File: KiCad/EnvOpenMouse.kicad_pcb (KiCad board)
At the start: 2 copper layers, 52.3 x 30.4 mm, 24 parts, among them J1 Conn_01x08, J2 Conn_01x03, J3 Conn_01x03, J4 Conn_01x03, SW1 SW_Push_SPDT, SW2 SW_Push_SPDT, U1 TCR2EF19, U2 PMW3360DM-T2QU

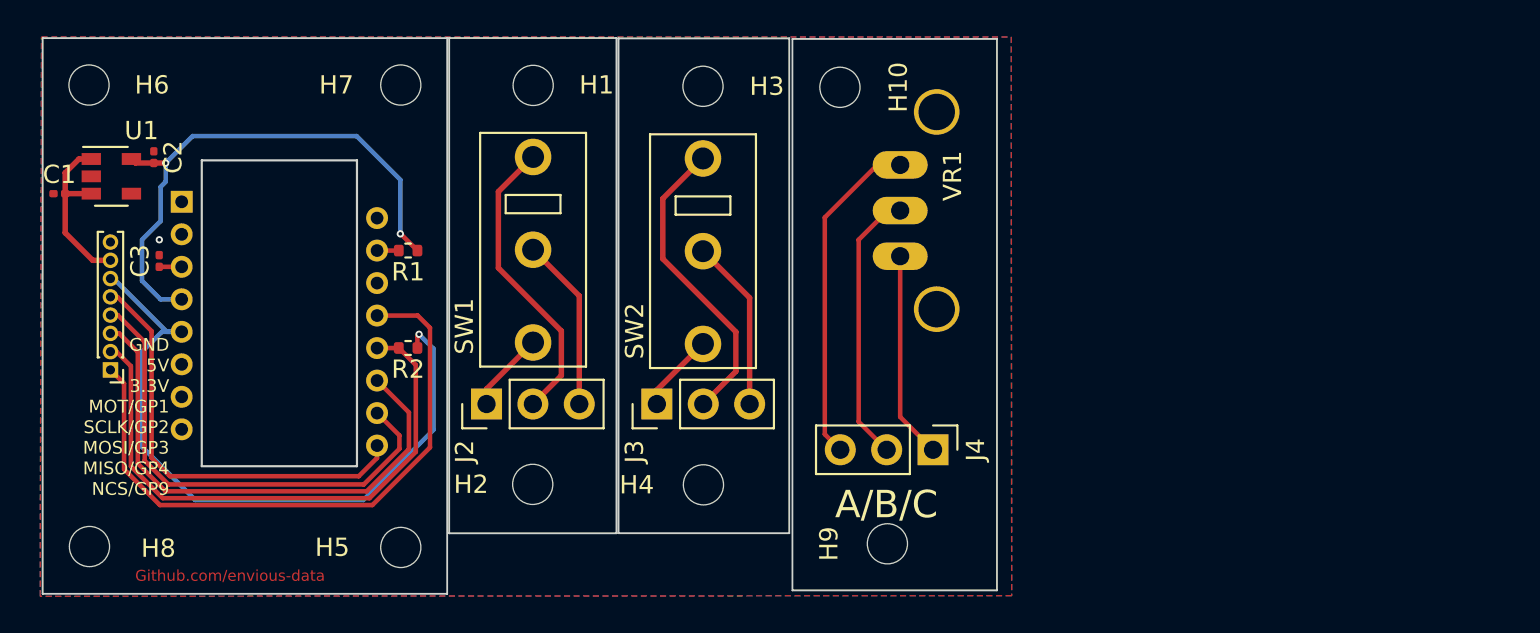
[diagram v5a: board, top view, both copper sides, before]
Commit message: added missing capactor and middle click button.
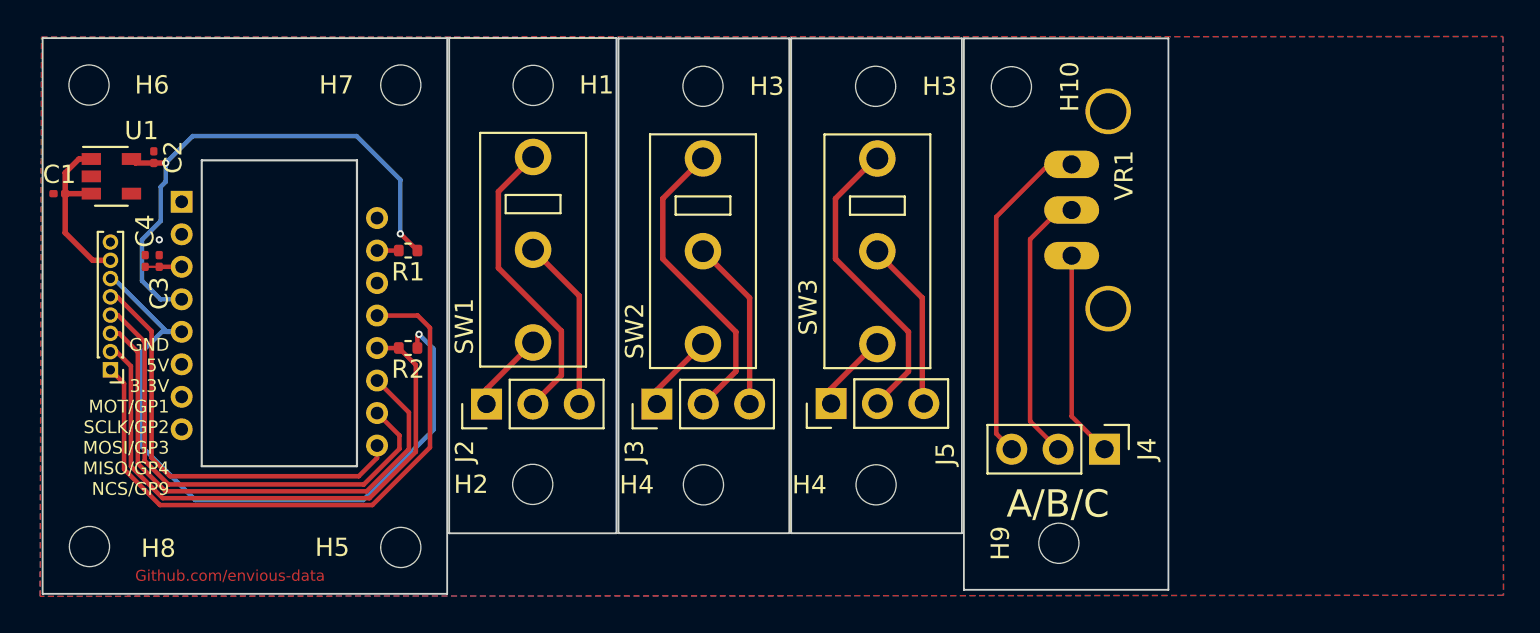
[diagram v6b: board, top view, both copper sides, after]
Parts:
- added C4: 100nf 0402, Capacitor_SMD:C_0201_0603Metric, F.Cu at (19.4, 24.6)
- added H3: MountingHole_Pad, MountingHole:MountingHole_2.2mm_M2, F.Cu at (59.5, 15.0)
- added H4: MountingHole_Pad, MountingHole:MountingHole_2.2mm_M2, F.Cu at (59.5, 36.8)
- added J5: Conn_01x03, Connector_PinHeader_2.54mm:PinHeader_1x03_P2.54mm_Vertical, F.Cu at (57.0, 32.4)
- added SW3: SW_Push_SPDT, MouseSwitch:MouseSwitch, F.Cu at (59.5, 24.0)
- moved H10 9.39 mm to (66.9, 15.0)
- moved VR1 9.39 mm to (70.2, 21.8)
- moved H9 9.39 mm to (69.5, 40.0)
- moved J4 9.39 mm to (72.0, 34.9)
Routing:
- net Net-(J5-Pad2): track 0.00 -> 16.8 mm
- net Net-(J5-Pad3): track 0.00 -> 9.43 mm
- net Net-(J5-Pad1): track 0.00 -> 4.34 mm
- net Net-(C3-Pad1): track 1.23 -> 2.00 mm
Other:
- board size 52.3 x 30.4 mm -> 61.7 x 30.4 mm

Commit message: Appended RP2040 to board, begin work on Mouse PCB
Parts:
- removed H10, H5, H6, H7, H8, H9: MountingHole_Pad, MountingHole:MountingHole_2.2mm_M2
- removed the H3 at (59.5, 15.0)
- removed the H3 at (50.0, 15.0)
- removed the H4 at (50.0, 36.8)
- removed the H4 at (59.5, 36.8)
- added C10: 100nf 0402, Capacitor_SMD:C_0402_1005Metric, F.Cu at (80.7, 85.0)
- added C11: 100nf 0402, Capacitor_SMD:C_0402_1005Metric, F.Cu at (77.8, 85.0)
- added C12: 100nf 0402, Capacitor_SMD:C_0402_1005Metric, F.Cu at (77.8, 87.0)
- added C13: 100nf 0402, Capacitor_SMD:C_0402_1005Metric, F.Cu at (66.9, 87.0)
- added C14: 100nf 0402, Capacitor_SMD:C_0402_1005Metric, F.Cu at (72.0, 85.7)
- added C15: 100nf 0402, Capacitor_SMD:C_0402_1005Metric, F.Cu at (80.0, 81.1)
- added C16: 100nf 0402, Capacitor_SMD:C_0402_1005Metric, F.Cu at (80.0, 83.1)
- added C17: 1uf 0402, Capacitor_SMD:C_0402_1005Metric, F.Cu at (72.0, 83.7)
- added C18: 1uf 0402, Capacitor_SMD:C_0402_1005Metric, F.Cu at (69.8, 87.6)
- added C19: 100nf 0402, Capacitor_SMD:C_0402_1005Metric, F.Cu at (61.2, 89.0)
- added C20: 10uf 0402, Capacitor_SMD:C_0402_1005Metric, F.Cu at (82.9, 82.2)
- added C21: 22pf 0402, Capacitor_SMD:C_0402_1005Metric, F.Cu at (64.0, 88.8)
- added C22: 22pf 0402, Capacitor_SMD:C_0402_1005Metric, F.Cu at (69.8, 89.6)
- added C5: 10uf 0402, Capacitor_SMD:C_0402_1005Metric, F.Cu at (69.2, 84.1)
- added C6: 10uf 0402, Capacitor_SMD:C_0402_1005Metric, F.Cu at (72.6, 87.6)
- added C7: 0.1uf 0402, Capacitor_SMD:C_0402_1005Metric, F.Cu at (66.9, 89.0)
- added C8: 100nf 0402, Capacitor_SMD:C_0402_1005Metric, F.Cu at (74.9, 85.7)
- added C9: 100nf 0402, Capacitor_SMD:C_0402_1005Metric, F.Cu at (74.9, 83.7)
- added CBP1: 10uf 0402, Capacitor_SMD:C_0402_1005Metric, F.Cu at (66.3, 85.0)
- added D1: 1N4002W, Diode_SMD:D_SOD-123, F.Cu at (51.6, 90.3)
- added F1: 0805L050WR, Fuse:Fuse_0805_2012Metric, F.Cu at (76.6, 74.7)
- added FB1: FerriteBead 0402, Resistor_SMD:R_0402_1005Metric, F.Cu at (77.1, 81.1)
- added FLASH1: W25Q16JVUXIQ, Package_SON:SON-8-1EP_3x2mm_P0.5mm_EP1.4x1.6mm, F.Cu at (72.1, 75.0)
- added GP23_LED1: GP23 LED_0402, LED_SMD:LED_0402_1005Metric, F.Cu at (84.5, 74.2)
- added GPIO24_RESISTOR1: 1K 0402, Resistor_SMD:R_0402_1005Metric, F.Cu at (68.4, 82.2)
- added GPIO25_LED1: LED_0402, LED_SMD:LED_0402_1005Metric, F.Cu at (87.7, 74.2)
- added GPIO25_RESISTOR1: 470 0402, Resistor_SMD:R_0402_1005Metric, F.Cu at (83.1, 78.2)
- added H3: MountingHole_Pad, MountingHole:MountingHole_2.2mm_M2, F.Cu at (122.8, 156.7)
- added H4: MountingHole_Pad, MountingHole:MountingHole_2.2mm_M2, F.Cu at (122.8, 162.6)
- added J8: TSA343G00-250J2, Button_Switch_SMD:SW_Push_SPST_NO_Alps_SKRK, F.Cu at (46.2, 85.1)
- added J9: Conn_01x03_Male, Connector_PinHeader_2.54mm:PinHeader_1x03_P2.54mm_Vertical, F.Cu at (55.9, 75.5)
- added NT1: NetTie_2, NetTie:NetTie-2_SMD_Pad0.5mm, F.Cu at (84.4, 76.2)
- added Q1: SI2301B, Package_TO_SOT_SMD:SOT-23, F.Cu at (67.3, 75.4)
- added R10: 10K 0402, Resistor_SMD:R_0402_1005Metric, F.Cu at (74.2, 81.7)
- added R11: 27r 0402 resistor, Resistor_SMD:R_0402_1005Metric, F.Cu at (77.3, 77.1)
- added R12: 27r 0402 resistor, Resistor_SMD:R_0402_1005Metric, F.Cu at (80.2, 77.1)
- added R13: 10K 0402, Resistor_SMD:R_0402_1005Metric, F.Cu at (71.5, 77.7)
- added R14: 1K 0402, Resistor_SMD:R_0402_1005Metric, F.Cu at (74.4, 77.7)
- added R15: 1K 0402, Resistor_SMD:R_0402_1005Metric, F.Cu at (65.5, 82.2)
- added R3: 5.1K 0402, Resistor_SMD:R_0402_1005Metric, F.Cu at (86.0, 79.2)
- added R4: 200 0603, Resistor_SMD:R_0603_1608Metric, F.Cu at (80.8, 74.4)
- added R5: 5.6K 0402, Resistor_SMD:R_0402_1005Metric, F.Cu at (71.3, 81.6)
- added R6: 1 0402, Resistor_SMD:R_0402_1005Metric, F.Cu at (83.1, 80.2)
- added R7: 5.1K 0402, Resistor_SMD:R_0402_1005Metric, F.Cu at (77.3, 79.1)
- added R8: 100K 0402, Resistor_SMD:R_0402_1005Metric, F.Cu at (80.2, 79.1)
- added R9: 220 0402, Resistor_SMD:R_0402_1005Metric, F.Cu at (74.2, 79.7)
- added RSW1: TSA343G00-250J2, Button_Switch_SMD:SW_Push_SPST_NO_Alps_SKRK, F.Cu at (61.5, 75.4)
- added TP1: TestPoint, EnvExtras:CustomTestPoint, F.Cu at (87.4, 76.7)
- added TP2: TestPoint, EnvExtras:CustomTestPoint, F.Cu at (68.5, 79.1)
- added TP3: TestPoint, EnvExtras:CustomTestPoint, F.Cu at (65.5, 79.7)
- added U3: SOT-23-5 5.5V 3.3V 500mA, Package_TO_SOT_SMD:SOT-23-5, F.Cu at (62.3, 85.6)
- added U4: RP2040, RP2040_minimal:RP2040-QFN-56, F.Cu at (38.3, 130.7)
- added USB1: TYPE-C-31-M-12, HRO-TYPE-C31-M-12:HRO-TYPE-C-31-M-12, F.Cu at (48.3, 82.1)
- added Y1: 3225_4P, Crystal:Crystal_SMD_3225-4Pin_3.2x2.5mm, F.Cu at (57.1, 90.8)
- C3: value 4.7uf 0402 -> 100nf 0402
- C4: value 100nf 0402 -> 4.7uf 0402
- U1: value TCR2EF19 -> TLV70218DBVR
- moved H1 166.1 mm to (116.8, 162.6)
- moved J3 144.6 mm to (92.1, 169.9)
- moved SW2 144.6 mm to (94.7, 161.5)
- moved H2 142.0 mm to (116.8, 156.7)
- moved C1 134.6 mm to (25.4, 155.0)
- moved C2 134.6 mm to (30.5, 153.0)
- moved C3 134.6 mm to (30.8, 158.7)
- moved C4 134.6 mm to (30.1, 158.7)
- moved J1 134.6 mm to (28.1, 164.7)
- moved R2 134.6 mm to (44.5, 163.5)
- moved R1 134.6 mm to (44.5, 158.1)
- moved U1 134.6 mm to (28.2, 154.1)
- moved U2 134.6 mm to (33.1, 153.9)
- moved J2 133.8 mm to (53.9, 165.3)
- moved SW1 133.8 mm to (56.5, 156.8)
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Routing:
- removed copper zone on B.Cu, net GND
- removed copper zone on F.Cu, net GND
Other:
- board size 61.7 x 30.4 mm -> 8.5 x 16.8 mm
- board text removed: "Github.com/envious-data"

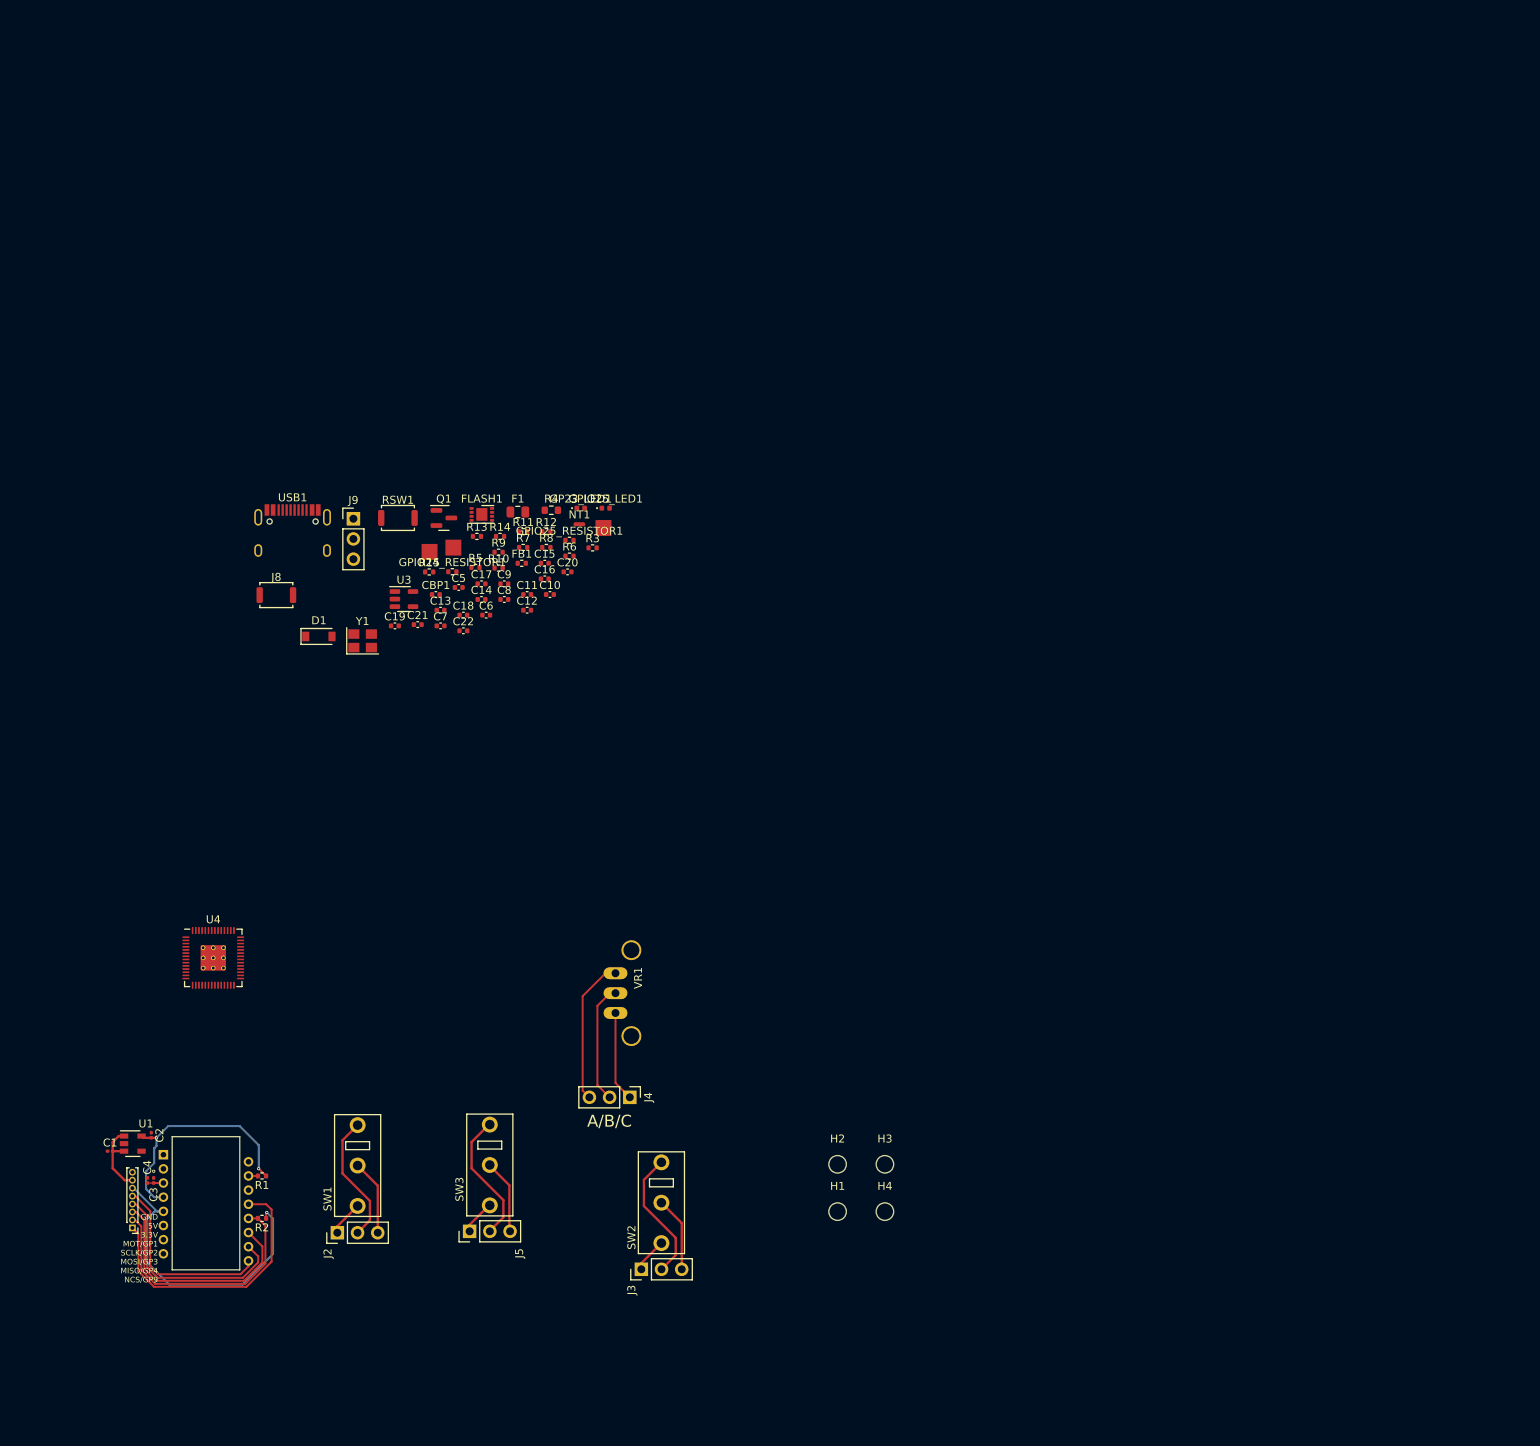
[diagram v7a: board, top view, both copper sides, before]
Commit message: routed onboard MCU
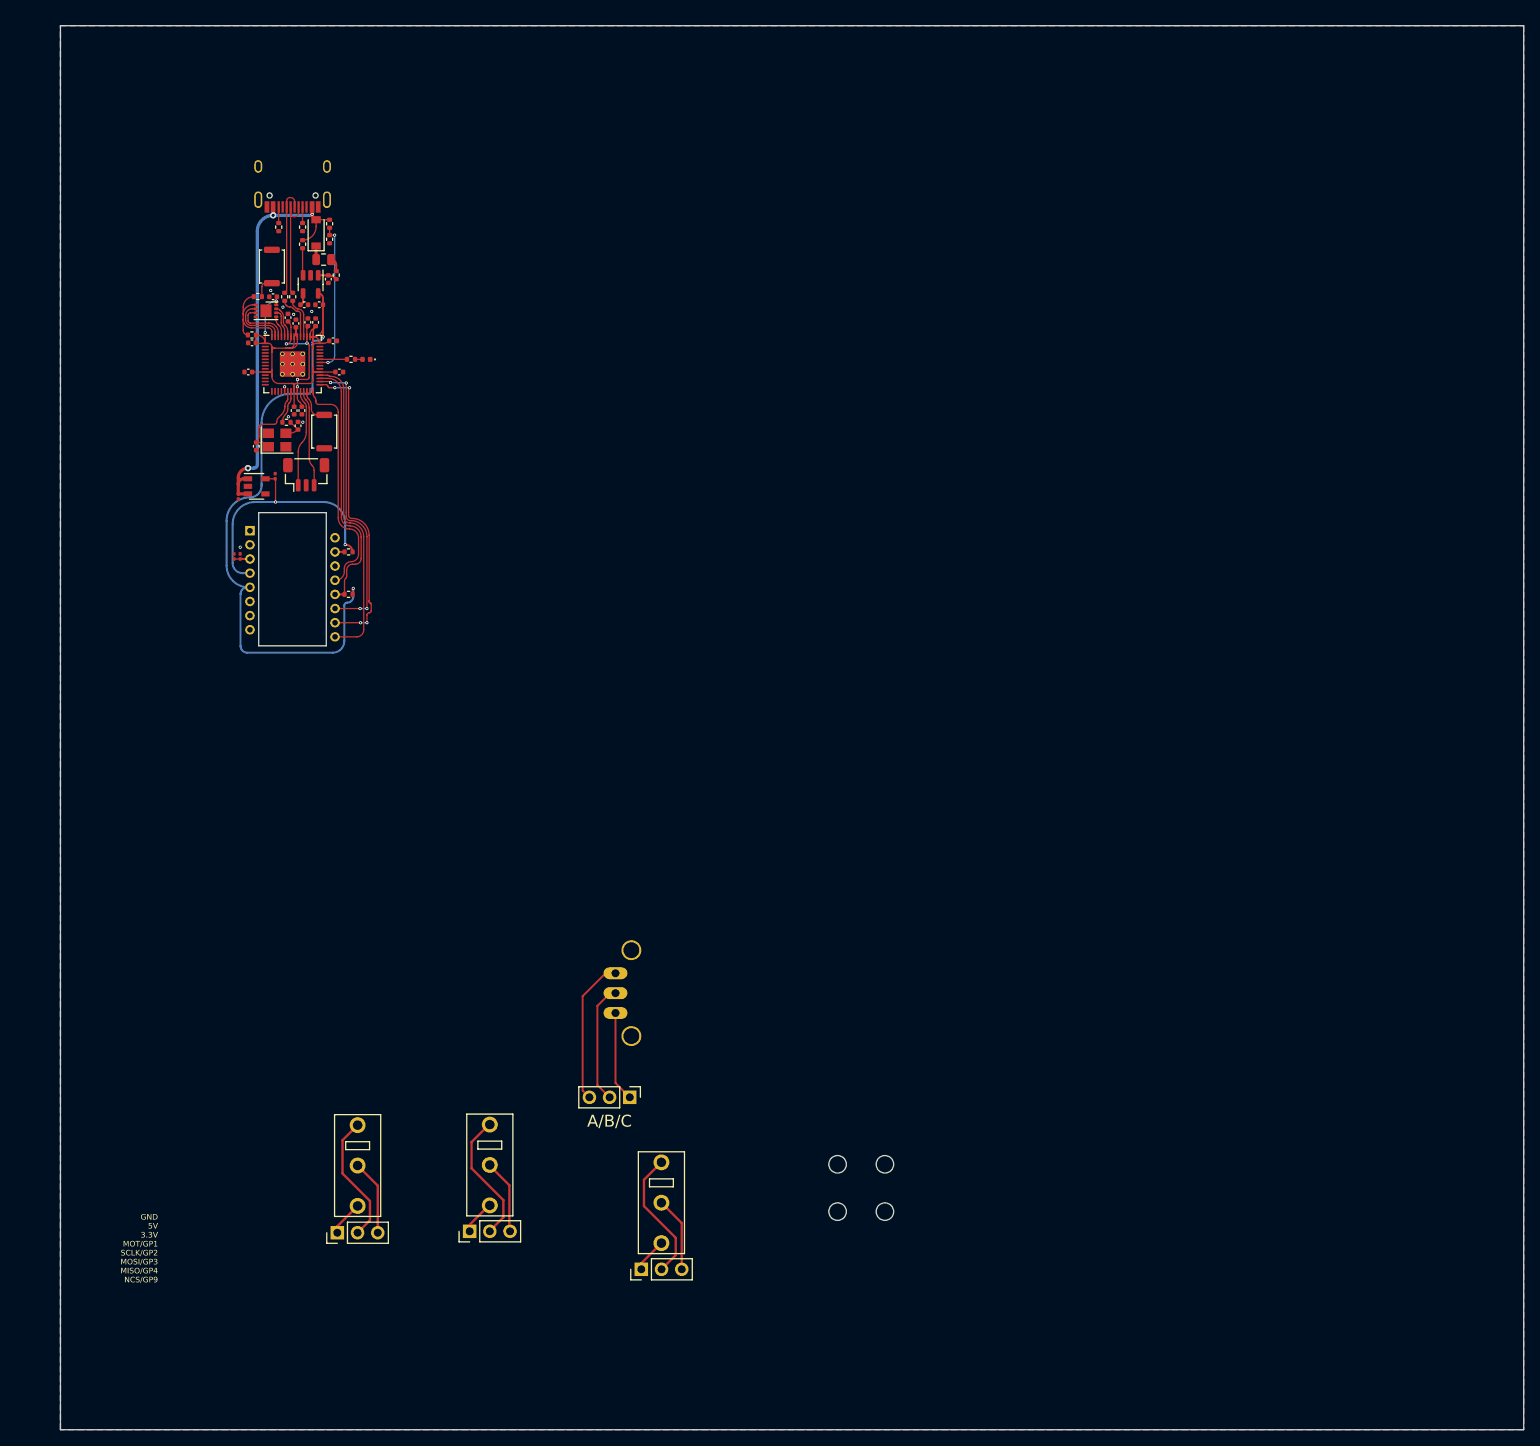
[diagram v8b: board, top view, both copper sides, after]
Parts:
- removed C16: 100nf 0402, Capacitor_SMD:C_0402_1005Metric
- removed C20: 10uf 0402, Capacitor_SMD:C_0402_1005Metric
- removed C7: 0.1uf 0402, Capacitor_SMD:C_0402_1005Metric
- removed GP23_LED1: GP23 LED_0402, LED_SMD:LED_0402_1005Metric
- removed GPIO24_RESISTOR1: 1K 0402, Resistor_SMD:R_0402_1005Metric
- removed J1: Conn_01x08, Connector_PinHeader_1.00mm:PinHeader_1x08_P1.00mm_Vertical
- removed NT1: NetTie_2, NetTie:NetTie-2_SMD_Pad0.5mm
- removed Q1: SI2301B, Package_TO_SOT_SMD:SOT-23
- removed R4: 200 0603, Resistor_SMD:R_0603_1608Metric
- removed R6: 1 0402, Resistor_SMD:R_0402_1005Metric
- removed R9: 220 0402, Resistor_SMD:R_0402_1005Metric
- removed TP1, TP2, TP3: TestPoint, EnvExtras:CustomTestPoint
- J9: value Conn_01x03_Male -> C145960; footprint Connector_PinHeader_2.54mm:PinHeader_1x03_P2.54mm_Vertical -> Connector_JST:JST_SH_BM03B-SRSS-TB_1x03-1MP_P1.00mm_Vertical
- moved C2 84.3 mm to (46.1, 70.2)
- moved U1 84.1 mm to (43.8, 71.4)
- moved C1 83.9 mm to (41.5, 72.7), turned to 90 degrees
- moved C3 79.2 mm to (41.7, 80.2)
- moved C4 79.2 mm to (40.9, 80.2)
- moved R1 79.2 mm to (55.3, 79.7)
- moved R2 79.2 mm to (55.3, 85.0)
- moved U2 79.2 mm to (44.0, 75.5)
- moved U4 75.3 mm to (48.3, 56.0)
- moved R3 54.4 mm to (49.5, 38.8), turned to 90 degrees
- moved USB1 53.5 mm to (48.3, 28.6), turned to 180 degrees
- moved D1 50.8 mm to (51.2, 39.5), turned to 90 degrees
- moved R7 50.7 mm to (46.5, 38.8), turned to 90 degrees
- moved R8 48.9 mm to (49.5, 41.0), turned to 90 degrees
- moved R5 46.9 mm to (53.0, 38.4), turned to -90 degrees
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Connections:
- C1 pad 2: +5V -> VBUS
- U1 pad 1: +5V -> VBUS
- U1 pad 3: +5V -> VBUS
- U4 pad 28: /RP2040/GPIO17 -> NCS/GPIO9
- U4 pad 29: /RP2040/GPIO18 -> SCLK/GPIO2
- U4 pad 30: /RP2040/GPIO19 -> MOSI/GPIO3
- U4 pad 31: /RP2040/GPIO20 -> MISO/GPIO4
- U4 pad 32: /RP2040/GPIO21 -> MOTION/GPIO1
- USB1 pad 13: Net-(C7-Pad2) -> GND
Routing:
- net +3V3: track 38.0 -> 139.5 mm, vias 1 -> 4
- net VBUS: track 0.00 -> 55.3 mm, vias 0 -> 3
- net /RP2040/GPIO24: track 0.00 -> 19.0 mm, vias 0 -> 2
- net +1V1: track 0.00 -> 17.7 mm, vias 0 -> 4
- net MOTION/GPIO1: track 23.8 -> 39.6 mm
- net USB_D-: track 0.00 -> 13.9 mm
- net USB_D+: track 0.00 -> 13.8 mm
- net /RP2040/QSPI_SS: track 0.00 -> 13.1 mm
- net SCLK/GPIO2: track 26.7 -> 39.7 mm, vias 0 -> 4
- net /RP2040/SWCLK: track 0.00 -> 12.3 mm
- net /RP2040/SWD: track 0.00 -> 12.1 mm
- net XIN: track 0.00 -> 10.6 mm
- net +5V: track 9.57 -> 0.00 mm
- net MOSI/GPIO3: track 28.9 -> 37.1 mm, vias 0 -> 4
- net /RP2040/QSPI_SD1: track 0.00 -> 7.39 mm
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- added copper zone on B.Cu, net GND
- added copper zone on F.Cu, net GND
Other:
- board size 8.5 x 16.8 mm -> 184 x 176.6 mm
